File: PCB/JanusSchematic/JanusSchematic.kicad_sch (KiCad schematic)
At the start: 8 parts, among them J1 USB_B_Micro, U1 MCP73832T-2ACI/OT

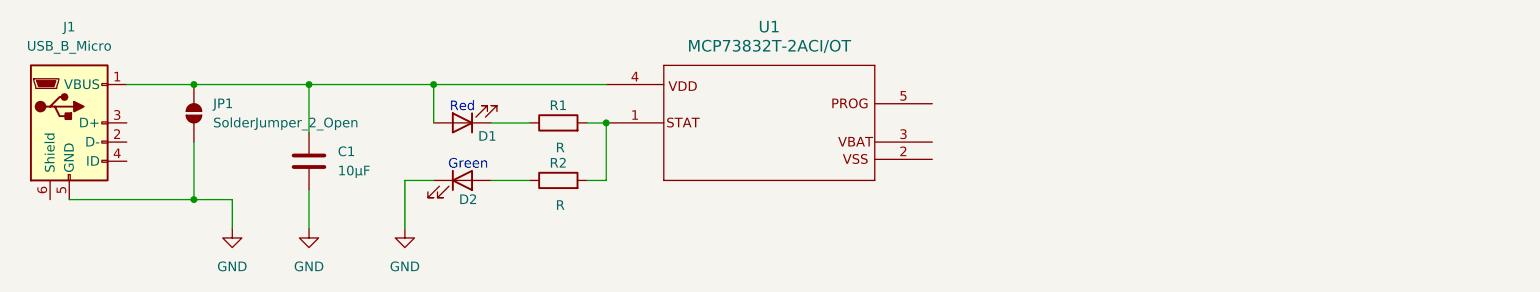
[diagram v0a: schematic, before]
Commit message: Finalized recharge circuit
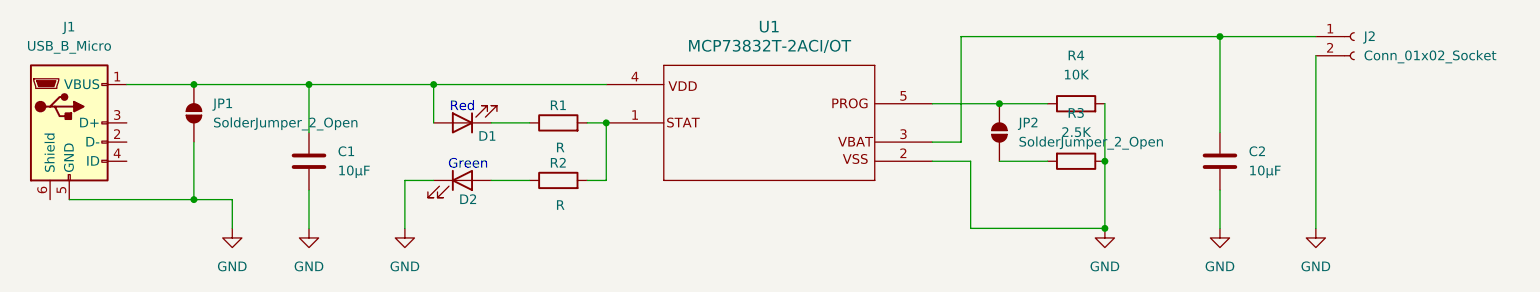
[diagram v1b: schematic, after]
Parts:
- added C2: 10μF, symbol Device:C
- added J2: Conn_01x02_Socket, symbol Connector:Conn_01x02_Socket
- added JP2: SolderJumper_2_Open, symbol Jumper:SolderJumper_2_Open
- added R3: 2.5K, symbol Device:R
- added R4: 10K, symbol Device:R
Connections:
- net GND: now also U1.2, C2.2, J2.2 (Pin_2), R3.1, R4.2
- net at U1.3: now also C2.1, J2.1 (Pin_1)
- net at U1.5: now also JP2.2 (B), R4.1
- new net: JP2.1 (A), R3.2
